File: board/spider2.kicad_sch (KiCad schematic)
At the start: 102 parts, among them J1 NRJ6HH-1, J10 PJ-320A, J11 PJ358, J12 PJ358, J13 PJ358, J14 PJ358, J15 PJ358, J16 PJ358, J17 USB4125, J19 PJ358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

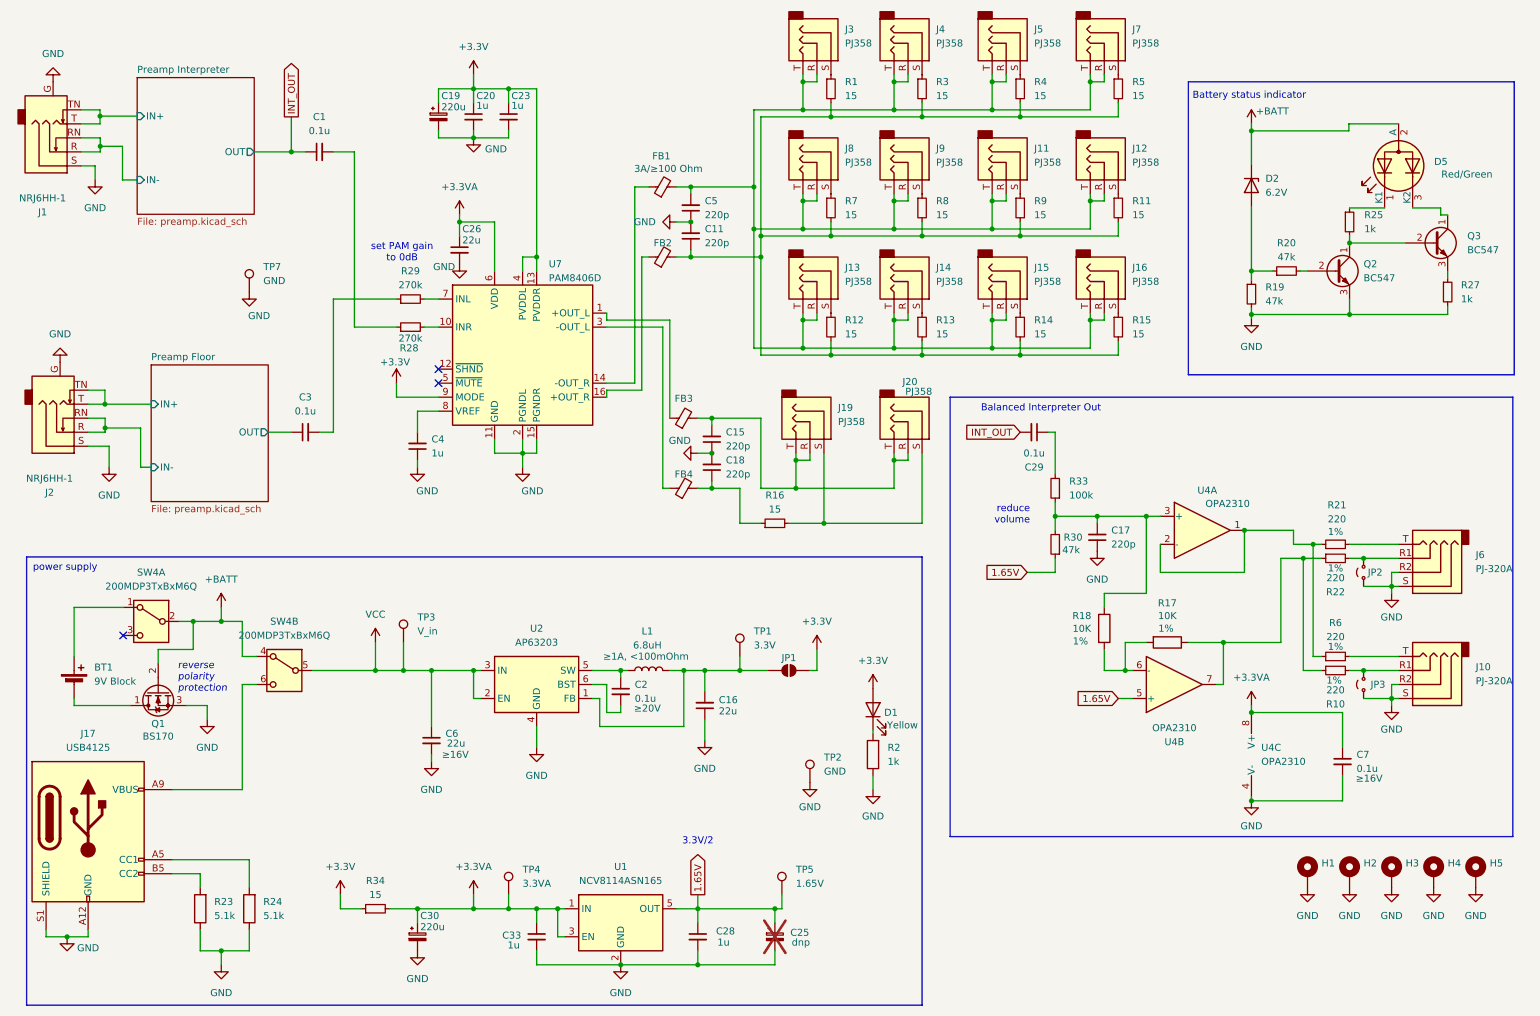
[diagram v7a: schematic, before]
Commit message: version 1.1b
almost identical to 1.1, but
- Limit Microphone Gain (R36,R46)
- Battery fuse
- More room for soldering USB port
- Correct footprints for 0.1uF capacitors
- Correct footprints for 4.7k resistor
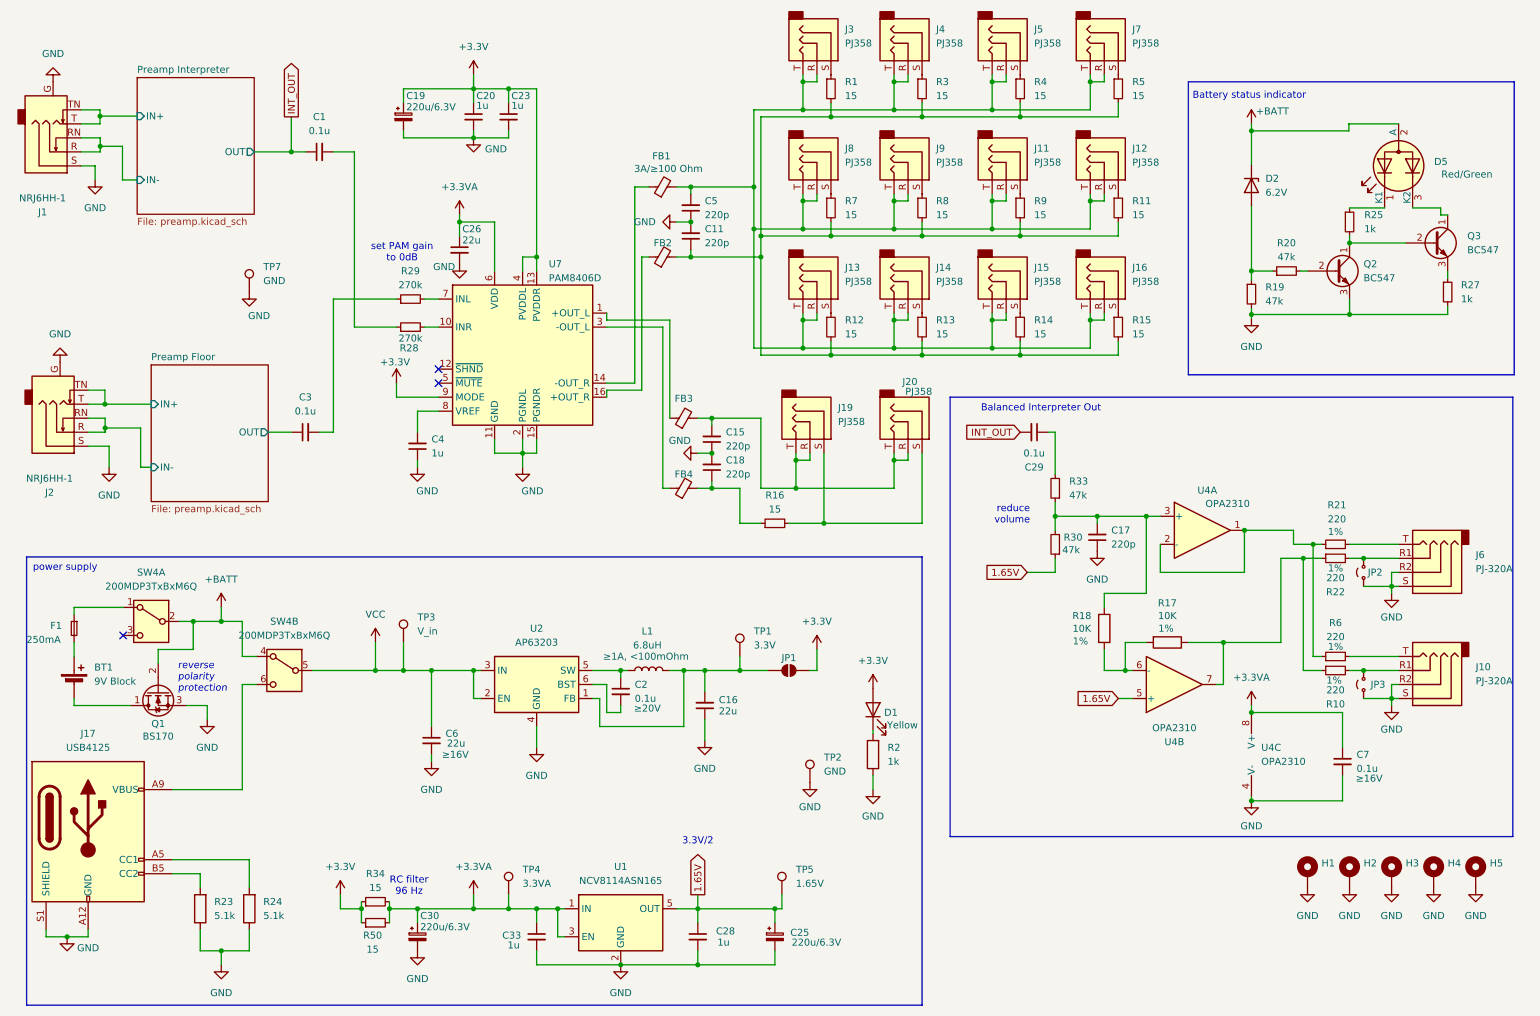
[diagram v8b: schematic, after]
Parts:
- added F1: 250mA, Fuse:Fuse_1206_3216Metric_Pad1.42x1.75mm_HandSolder, symbol Device:Fuse_Small
- added R50: 15, Resistor_THT:R_Axial_DIN0207_L6.3mm_D2.5mm_P10.16mm_Horizontal, symbol Device:R_Small
- C1, C20, C23, C28, C29, C3, C33, C4, C7: footprint Capacitor_THT:C_Disc_D4.3mm_W1.9mm_P5.00mm -> Capacitor_THT:C_Disc_D3.0mm_W2.0mm_P2.50mm
- C19, C30: value 220u -> 220u/6.3V
- C25: value dnp -> 220u/6.3V; now fitted
- R33: value 100k -> 47k
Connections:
- net +3.3V: now also R50.1
- net +3.3VA: now also R50.2
- net at SW4.1 (A): now also F1.1; no longer BT1.1 (+)
- new net: BT1.1 (+), F1.2
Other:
- note added: "RC filter 96 Hz"
- moved on the sheet: C19
